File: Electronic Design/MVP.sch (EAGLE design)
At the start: 36 parts, among them IC1 ACS711KLCTR-12AB-T, IC3 ATMEGA328-PU, Q2 16MHz, Q3 IRF9540, Q4 IRF9540

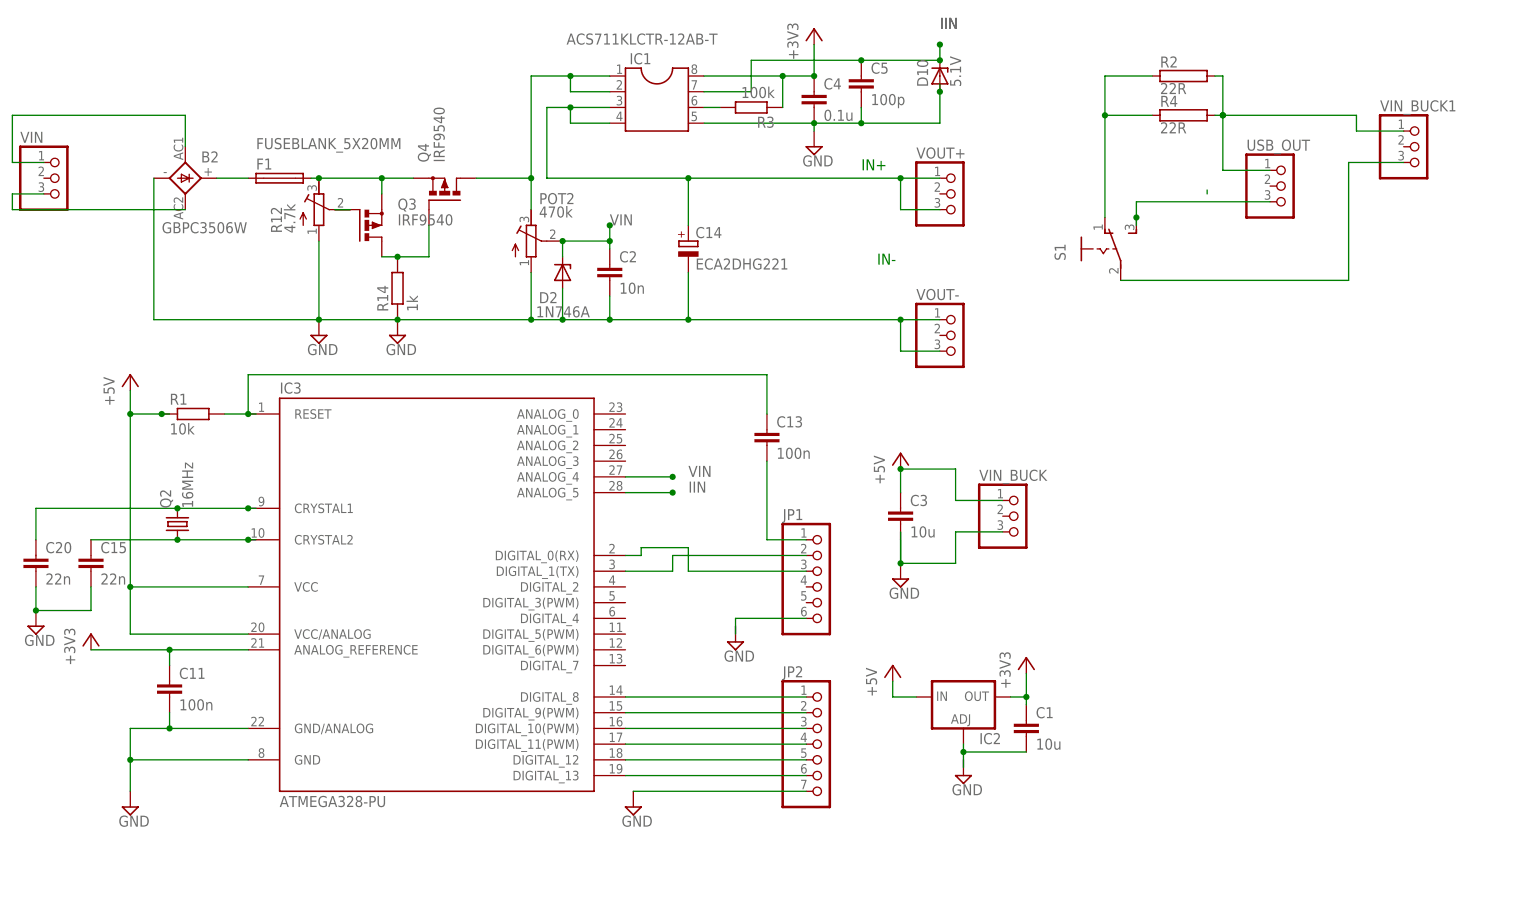
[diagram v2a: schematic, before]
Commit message: Adding components needed for current offset calibrations
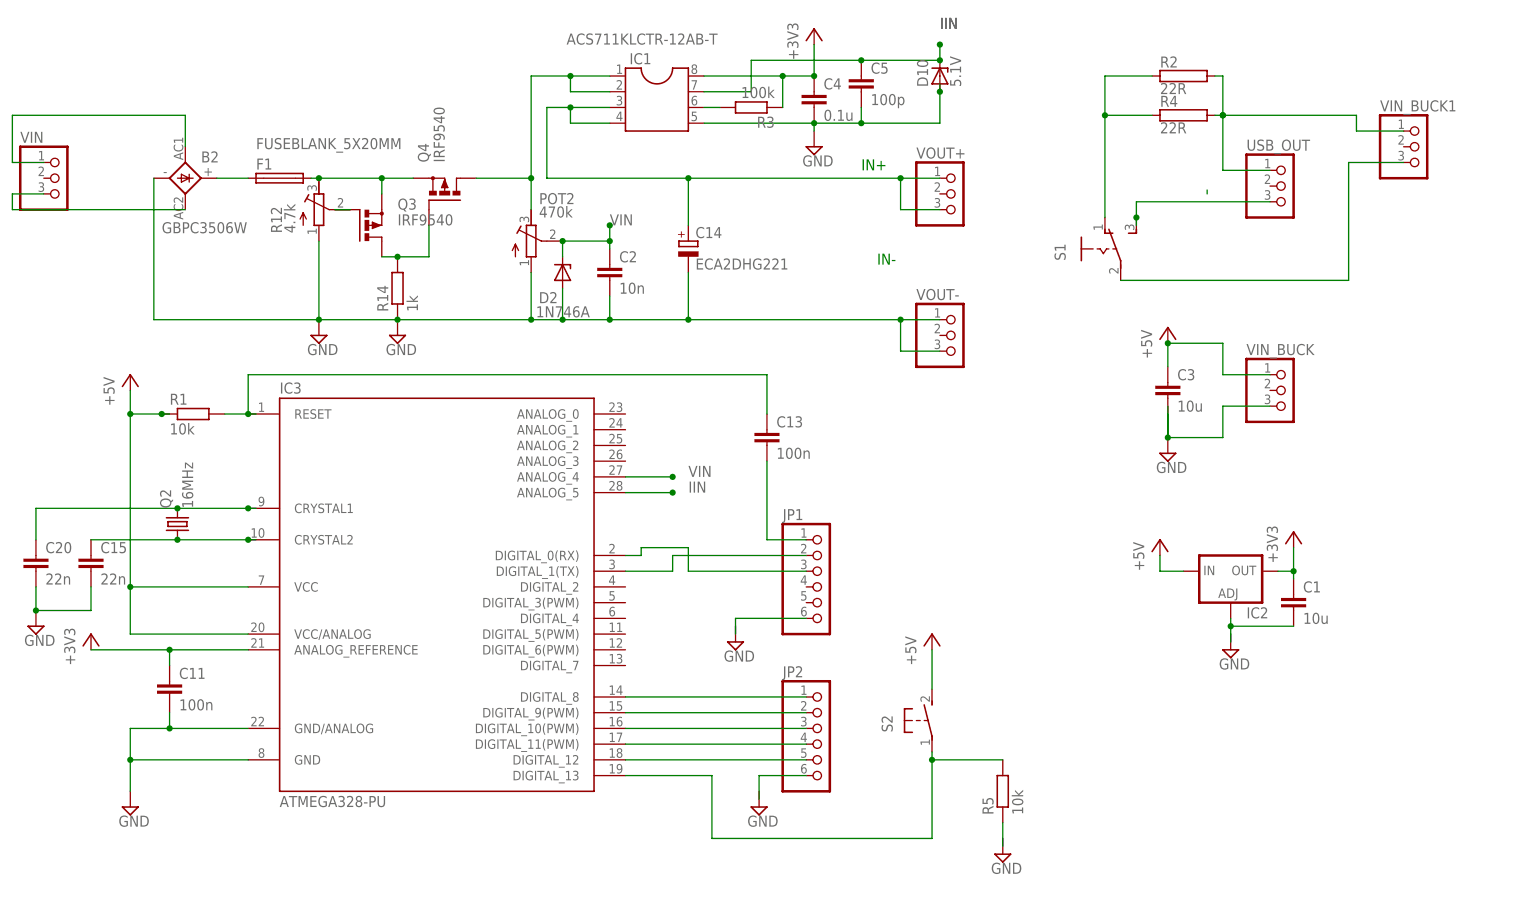
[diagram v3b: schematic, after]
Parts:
- added R5: 10k, resistor:R-EU_R1210
- added S2: (no value), switch-omron:31-XX
- JP2: device pinhead:PINHD-1X7 -> pinhead:PINHD-1X6
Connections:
- new net N$26: R5.1
- new net N$27: JP2.6
- net +5V: now also S2.S
- net GND: no longer JP2.7
- net N$8: now also R5.2, S2.P; no longer JP2.6
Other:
- moved on the sheet: C1, C3, IC2, VIN_BUCK
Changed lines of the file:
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@@
 <part name="SUPPLY14" library="supply2" deviceset="GND" device=""/>
 <part name="SUPPLY17" library="supply2" deviceset="GND" device=""/>
-<part name="JP2" library="pinhead" deviceset="PINHD-1X7" device=""/>
+<part name="JP2" library="pinhead" deviceset="PINHD-1X6" device=""/>
 <part name="VOUT-" library="pinhead" deviceset="PINHD-1X3" device=""/>
 <part name="VIN_BUCK" library="pinhead" deviceset="PINHD-1X3" device=""/>
@@
 <part name="S1" library="switch" deviceset="255SB" device=""/>
 <part name="USB_OUT" library="pinhead" deviceset="PINHD-1X3" device=""/>
+<part name="S2" library="switch-omron" deviceset="31-XX" device=""/>
+<part name="+5V2" library="supply1" deviceset="+5V" device=""/>
+<part name="R5" library="resistor" deviceset="R-EU_" device="R1210" value="10k"/>
+<part name="SUPPLY3" library="supply2" deviceset="GND" device=""/>
 </parts>
 <sheets>
@@
 <instance part="C20" gate="G$1" x="-107.95" y="27.94"/>
 <instance part="SUPPLY14" gate="GND" x="-107.95" y="16.51"/>
-<instance part="SUPPLY17" gate="GND" x="-11.43" y="-12.7"/>
+<instance part="SUPPLY17" gate="GND" x="8.89" y="-12.7"/>
 <instance part="JP2" gate="A" x="19.05" y="-2.54"/>
 <instance part="VOUT-" gate="A" x="40.64" y="63.5"/>
-<instance part="VIN_BUCK" gate="A" x="50.8" y="34.29"/>
-<instance part="SUPPLY2" gate="GND" x="31.75" y="24.13"/>
-<instance part="+3V2" gate="1" x="31.75" y="44.45"/>
-<instance part="IC2" gate="G$1" x="41.91" y="5.08"/>
-<instance part="SUPPLY5" gate="GND" x="41.91" y="-7.62"/>
-<instance part="+3V3" gate="1" x="30.48" y="10.16"/>
-<instance part="+3V4" gate="G$1" x="52.07" y="11.43"/>
-<instance part="C1" gate="G$1" x="52.07" y="1.27"/>
+<instance part="VIN_BUCK" gate="A" x="93.98" y="54.61"/>
+<instance part="SUPPLY2" gate="GND" x="74.93" y="44.45"/>
+<instance part="+3V2" gate="1" x="74.93" y="64.77"/>
+<instance part="IC2" gate="G$1" x="85.09" y="25.4"/>
+<instance part="SUPPLY5" gate="GND" x="85.09" y="12.7"/>
+<instance part="+3V3" gate="1" x="73.66" y="30.48"/>
+<instance part="+3V4" gate="G$1" x="95.25" y="31.75"/>
+<instance part="C1" gate="G$1" x="95.25" y="21.59"/>
 <instance part="+3V1" gate="G$1" x="17.78" y="113.03"/>
 <instance part="+3V5" gate="G$1" x="-99.06" y="15.24"/>
 <instance part="JP1" gate="A" x="19.05" y="22.86"/>
 <instance part="SUPPLY6" gate="GND" x="5.08" y="13.97"/>
-<instance part="C3" gate="G$1" x="31.75" y="35.56"/>
+<instance part="C3" gate="G$1" x="74.93" y="55.88"/>
 <instance part="VIN_BUCK1" gate="A" x="115.57" y="93.98"/>
 <instance part="R2" gate="G$1" x="77.47" y="105.41"/>
@@
 <instance part="S1" gate="1" x="64.77" y="77.47"/>
 <instance part="USB_OUT" gate="A" x="93.98" y="87.63"/>
+<instance part="S2" gate="1" x="36.83" y="1.27"/>
+<instance part="+5V2" gate="1" x="36.83" y="15.24"/>
+<instance part="R5" gate="G$1" x="48.26" y="-10.16" rot="R90"/>
+<instance part="SUPPLY3" gate="GND" x="48.26" y="-20.32"/>
 </instances>
 <busses>
@@
 </segment>
 <segment>
-<pinref part="SUPPLY17" gate="GND" pin="GND"/>
-<pinref part="JP2" gate="A" pin="7"/>
-<wire x1="-11.43" y1="-10.16" x2="16.51" y2="-10.16" width="0.1524" layer="91"/>
-</segment>
-<segment>
 <pinref part="SUPPLY2" gate="GND" pin="GND"/>
-<wire x1="31.75" y1="31.75" x2="31.75" y2="26.67" width="0.1524" layer="91"/>
+<wire x1="74.93" y1="52.07" x2="74.93" y2="46.99" width="0.1524" layer="91"/>
 <pinref part="C3" gate="G$1" pin="2"/>
-<junction x="31.75" y="26.67"/>
-<wire x1="31.75" y1="26.67" x2="31.75" y2="30.48" width="0.1524" layer="91"/>
-<wire x1="31.75" y1="26.67" x2="40.64" y2="26.67" width="0.1524" layer="91"/>
-<wire x1="40.64" y1="26.67" x2="40.64" y2="31.75" width="0.1524" layer="91"/>
+<junction x="74.93" y="46.99"/>
+<wire x1="74.93" y1="46.99" x2="74.93" y2="50.8" width="0.1524" layer="91"/>
+<wire x1="74.93" y1="46.99" x2="83.82" y2="46.99" width="0.1524" layer="91"/>
+<wire x1="83.82" y1="46.99" x2="83.82" y2="52.07" width="0.1524" layer="91"/>
 <pinref part="VIN_BUCK" gate="A" pin="3"/>
-<wire x1="40.64" y1="31.75" x2="48.26" y2="31.75" width="0.1524" layer="91"/>
+<wire x1="83.82" y1="52.07" x2="91.44" y2="52.07" width="0.1524" layer="91"/>
 </segment>
 <segment>
 <pinref part="IC2" gate="G$1" pin="ADJ"/>
-<wire x1="41.91" y1="-2.54" x2="41.91" y2="-3.81" width="0.1524" layer="91"/>
+<wire x1="85.09" y1="17.78" x2="85.09" y2="16.51" width="0.1524" layer="91"/>
 <pinref part="C1" gate="G$1" pin="2"/>
-<wire x1="41.91" y1="-3.81" x2="41.91" y2="-5.08" width="0.1524" layer="91"/>
-<wire x1="41.91" y1="-5.08" x2="41.91" y2="-6.35" width="0.1524" layer="91"/>
-<wire x1="52.07" y1="-3.81" x2="41.91" y2="-3.81" width="0.1524" layer="91"/>
-<junction x="41.91" y="-3.81"/>
+<wire x1="85.09" y1="16.51" x2="85.09" y2="15.24" width="0.1524" layer="91"/>
+<wire x1="85.09" y1="15.24" x2="85.09" y2="13.97" width="0.1524" layer="91"/>
+<wire x1="95.25" y1="16.51" x2="85.09" y2="16.51" width="0.1524" layer="91"/>
+<junction x="85.09" y="16.51"/>
 <pinref part="SUPPLY5" gate="GND" pin="GND"/>
 </segment>
@@
 <pinref part="+3V2" gate="1" pin="+5V"/>
 <pinref part="C3" gate="G$1" pin="1"/>
-<junction x="31.75" y="41.91"/>
-<wire x1="31.75" y1="41.91" x2="31.75" y2="38.1" width="0.1524" layer="91"/>
-<wire x1="31.75" y1="41.91" x2="40.64" y2="41.91" width="0.1524" layer="91"/>
-<wire x1="40.64" y1="41.91" x2="40.64" y2="36.83" width="0.1524" layer="91"/>
+<junction x="74.93" y="62.23"/>
+<wire x1="74.93" y1="62.23" x2="74.93" y2="58.42" width="0.1524" layer="91"/>
+<wire x1="74.93" y1="62.23" x2="83.82" y2="62.23" width="0.1524" layer="91"/>
+<wire x1="83.82" y1="62.23" x2="83.82" y2="57.15" width="0.1524" layer="91"/>
 <pinref part="VIN_BUCK" gate="A" pin="1"/>
-<wire x1="40.64" y1="36.83" x2="48.26" y2="36.83" width="0.1524" layer="91"/>
+<wire x1="83.82" y1="57.15" x2="91.44" y2="57.15" width="0.1524" layer="91"/>
 </segment>
 <segment>
 <pinref part="IC2" gate="G$1" pin="IN"/>
 <pinref part="+3V3" gate="1" pin="+5V"/>
-<wire x1="34.29" y1="5.08" x2="30.48" y2="5.08" width="0.1524" layer="91"/>
-<wire x1="30.48" y1="5.08" x2="30.48" y2="7.62" width="0.1524" layer="91"/>
+<wire x1="77.47" y1="25.4" x2="73.66" y2="25.4" width="0.1524" layer="91"/>
+<wire x1="73.66" y1="25.4" x2="73.66" y2="27.94" width="0.1524" layer="91"/>
+</segment>
+<segment>
+<pinref part="S2" gate="1" pin="S"/>
+<pinref part="+5V2" gate="1" pin="+5V"/>
+<wire x1="36.83" y1="6.35" x2="36.83" y2="12.7" width="0.1524" layer="91"/>
 </segment>
 </net>
@@
 <segment>
 <pinref part="IC3" gate="1" pin="DIGITAL_13"/>
-<pinref part="JP2" gate="A" pin="6"/>
-<wire x1="-12.7" y1="-7.62" x2="16.51" y2="-7.62" width="0.1524" layer="91"/>
+<wire x1="-12.7" y1="-7.62" x2="1.27" y2="-7.62" width="0.1524" layer="91"/>
+<wire x1="1.27" y1="-7.62" x2="1.27" y2="-17.78" width="0.1524" layer="91"/>
+<pinref part="S2" gate="1" pin="P"/>
+<wire x1="1.27" y1="-17.78" x2="36.83" y2="-17.78" width="0.1524" layer="91"/>
+<wire x1="36.83" y1="-17.78" x2="36.83" y2="-5.08" width="0.1524" layer="91"/>
+<pinref part="R5" gate="G$1" pin="2"/>
+<wire x1="36.83" y1="-5.08" x2="36.83" y2="-3.81" width="0.1524" layer="91"/>
+<wire x1="48.26" y1="-5.08" x2="36.83" y2="-5.08" width="0.1524" layer="91"/>
+<junction x="36.83" y="-5.08"/>
 </segment>
 </net>
@@
 <pinref part="IC2" gate="G$1" pin="OUT"/>
 <pinref part="+3V4" gate="G$1" pin="+3V3"/>
-<wire x1="49.53" y1="5.08" x2="52.07" y2="5.08" width="0.1524" layer="91"/>
-<wire x1="52.07" y1="5.08" x2="52.07" y2="8.89" width="0.1524" layer="91"/>
+<wire x1="92.71" y1="25.4" x2="95.25" y2="25.4" width="0.1524" layer="91"/>
+<wire x1="95.25" y1="25.4" x2="95.25" y2="29.21" width="0.1524" layer="91"/>
 <pinref part="C1" gate="G$1" pin="1"/>
-<wire x1="52.07" y1="3.81" x2="52.07" y2="5.08" width="0.1524" layer="91"/>
-<junction x="52.07" y="5.08"/>
+<wire x1="95.25" y1="24.13" x2="95.25" y2="25.4" width="0.1524" layer="91"/>
+<junction x="95.25" y="25.4"/>
 </segment>
 <segment>
@@
 </segment>
 </net>
+<net name="N$26" class="0">
+<segment>
+<pinref part="R5" gate="G$1" pin="1"/>
+<wire x1="48.26" y1="-15.24" x2="48.26" y2="-19.05" width="0.1524" layer="91"/>
+</segment>
+</net>
+<net name="N$27" class="0">
+<segment>
+<pinref part="JP2" gate="A" pin="6"/>
+<wire x1="16.51" y1="-7.62" x2="8.89" y2="-7.62" width="0.1524" layer="91"/>
+<wire x1="8.89" y1="-7.62" x2="8.89" y2="-11.43" width="0.1524" layer="91"/>
+</segment>
+</net>

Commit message: Updating changes to schematics as well as adding BOM .txt file
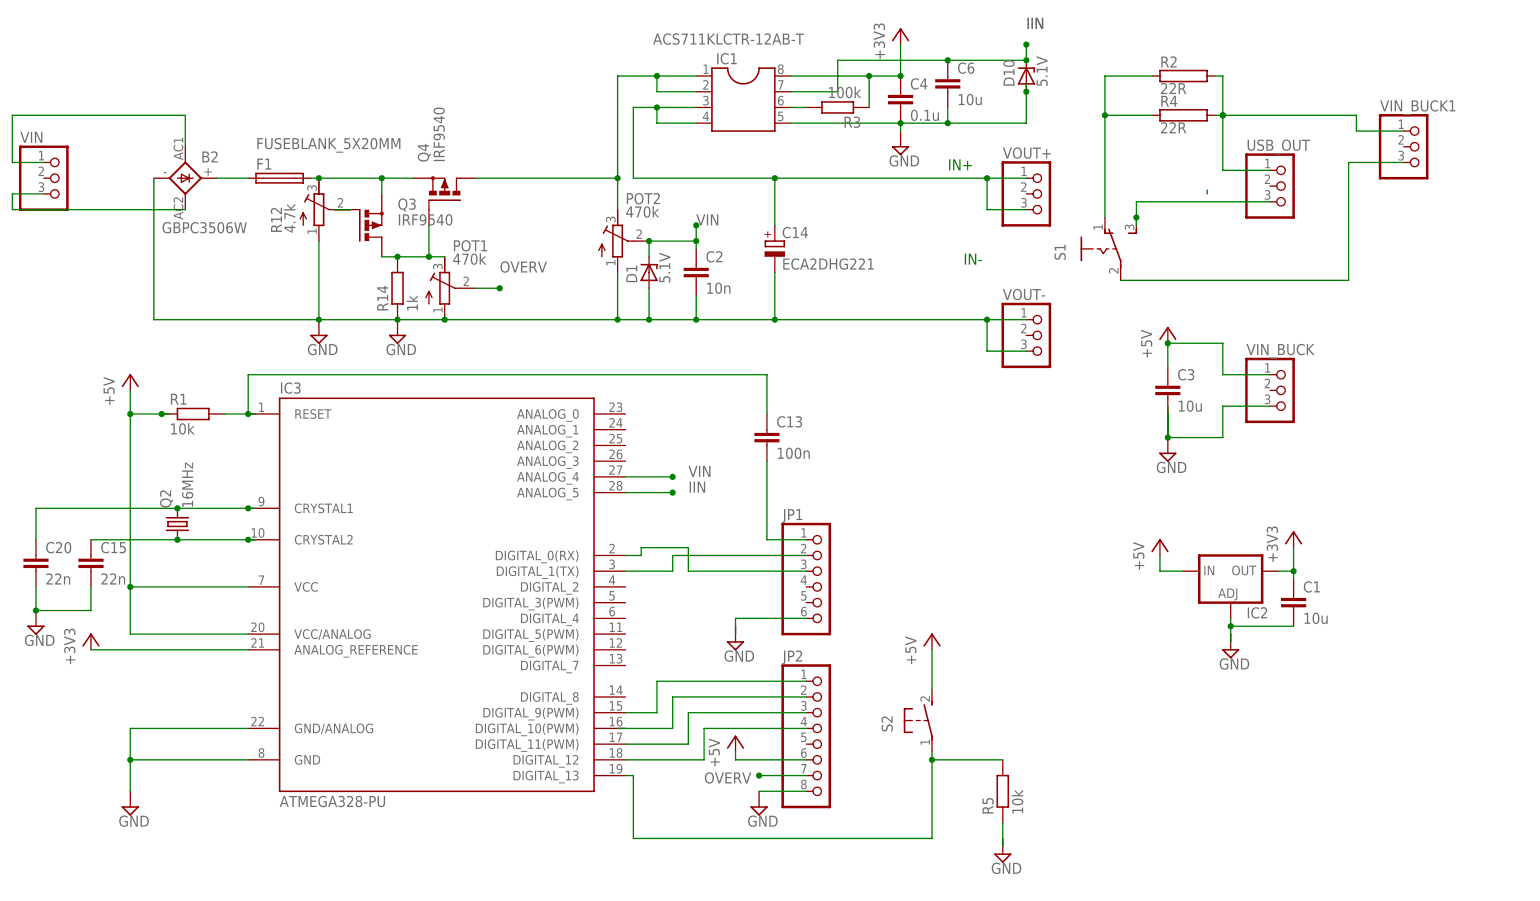
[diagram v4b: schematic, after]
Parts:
- removed C11: 100n, resistor:C-EUC1210
- removed C5: 100p, resistor:C-EUC1210
- removed D2: 1N746A, diode:ZENER-DIODEDO34-7
- added C6: 10u, resistor:C-EUC1210
- added D1: 5.1V, diode:ZPD
- added POT1: 470k, resistor:R-TRIMM4G/J
- JP2: device pinhead:PINHD-1X6 -> pinhead:PINHD-1X8
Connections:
- removed net N$13: IC3.DIGITAL_12, JP2.5
- removed net N$27: JP2.6
- new net OVERV: JP2.7, POT1.S
- net +3V3: no longer C11.1
- net +5V: now also JP2.6
- net GND: now also C6.2, D1.A, JP2.8, POT1.A; no longer C11.2, C5.2, D2.A
- net IIN: now also C6.1; no longer C5.1
- net N$11: now also IC3.DIGITAL_11(PWM); no longer IC3.DIGITAL_10(PWM)
- net N$12: now also IC3.DIGITAL_12; no longer IC3.DIGITAL_11(PWM)
- net N$35: now also POT1.E
- net N$6: now also JP2.1; no longer JP2.2
- net N$9: now also JP2.2; no longer IC3.DIGITAL_8, JP2.1
- net VIN: now also D1.C; no longer D2.C
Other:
- moved on the sheet: C14, C2, C4, D10, IC1, POT2, R3, VOUT+, VOUT-
